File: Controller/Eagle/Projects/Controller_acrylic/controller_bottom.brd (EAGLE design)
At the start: 280.8 x 115 mm, 4 parts

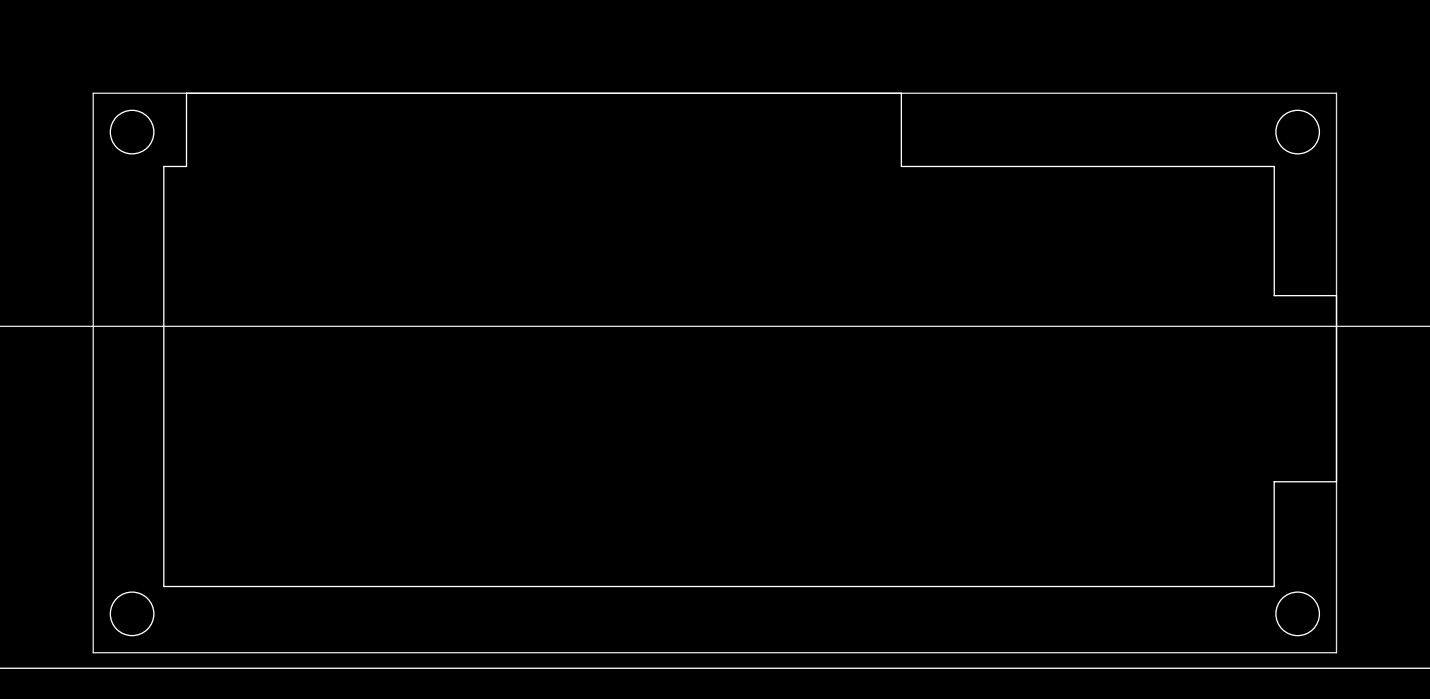
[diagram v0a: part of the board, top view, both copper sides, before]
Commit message: Now it should be ready controller_bottom was not supposed to have the LCD cutout Added dimension to layer 20 in connector board
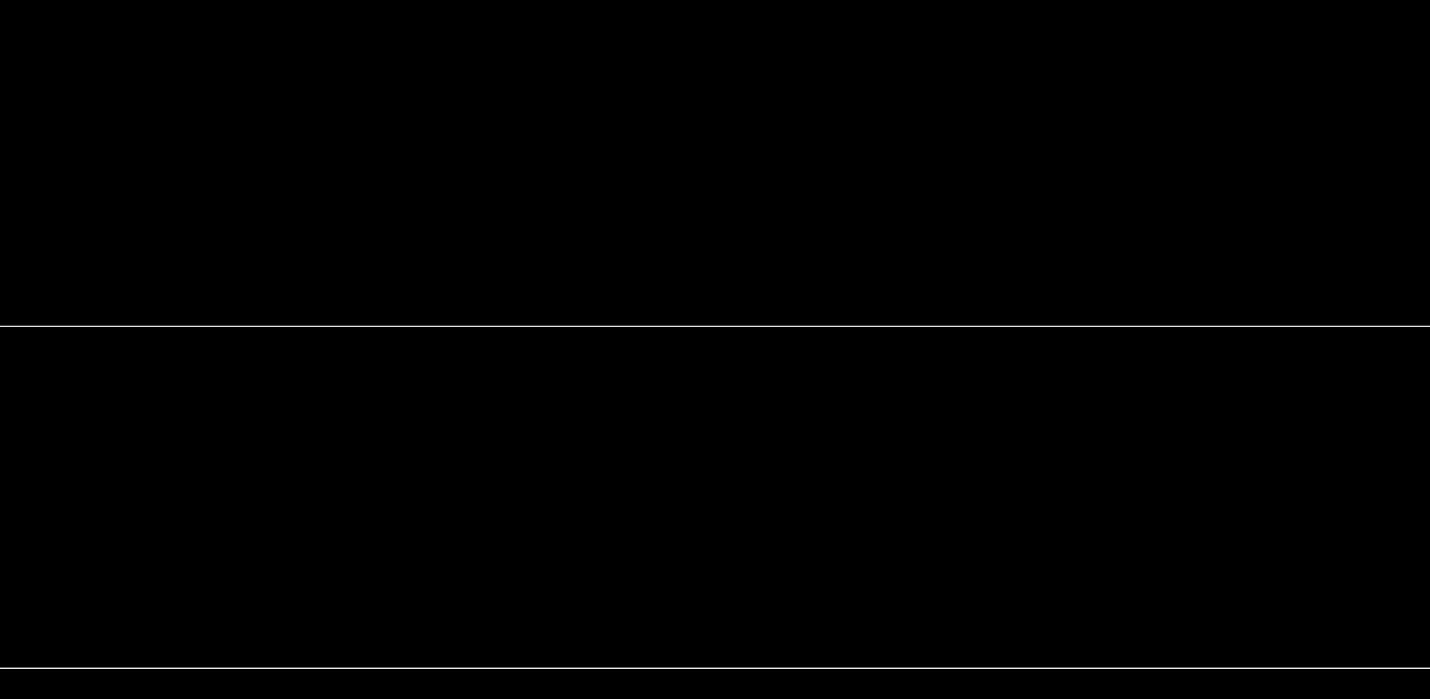
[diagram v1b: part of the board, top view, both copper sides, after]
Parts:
- removed U$4: (no value), Controller:SPARKFUN_LCD_33

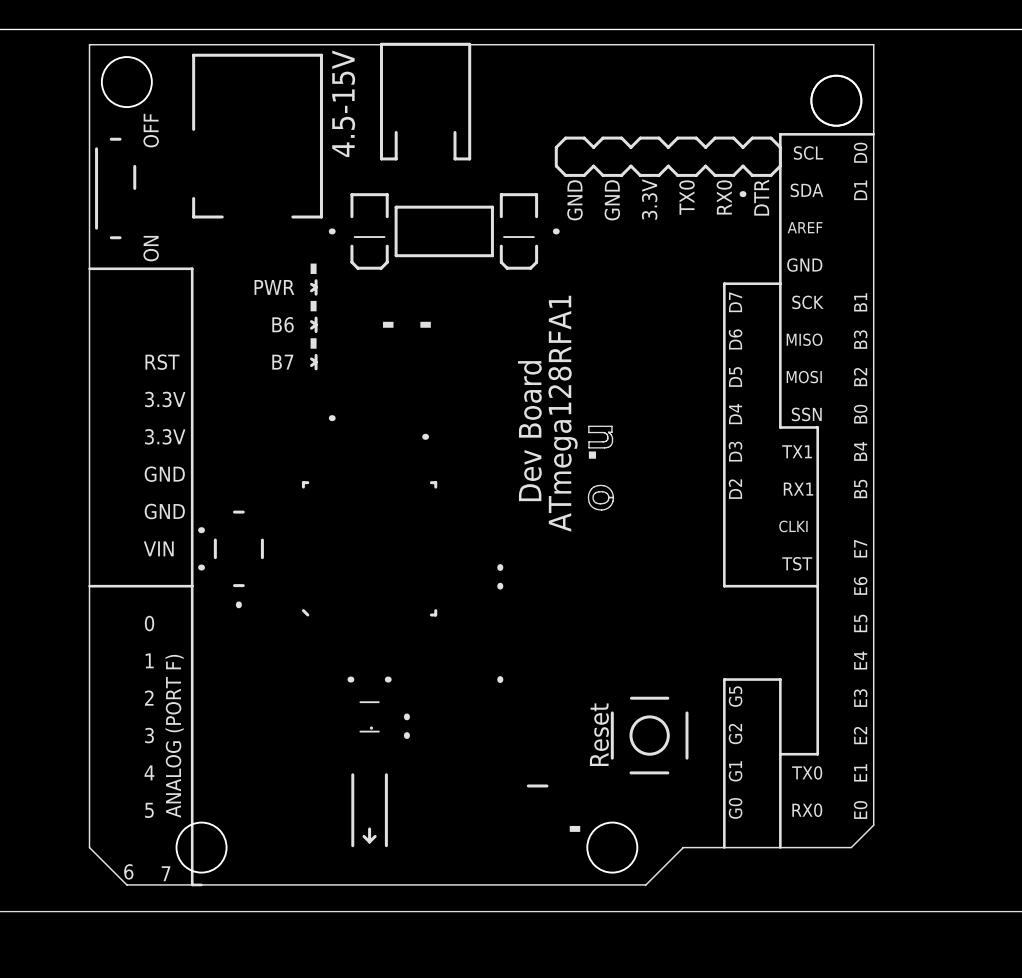
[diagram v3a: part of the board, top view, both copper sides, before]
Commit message: Nudged sparkfun board to the right a bit to make room for battery pack
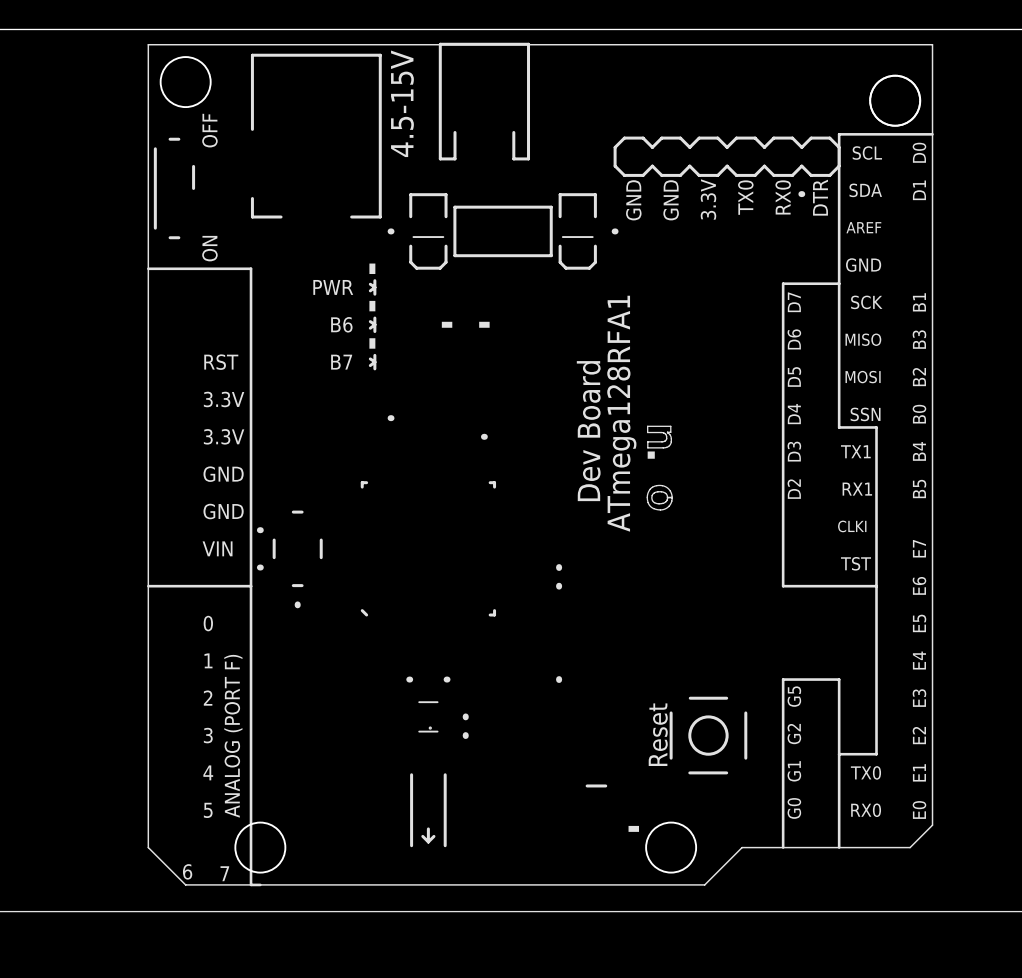
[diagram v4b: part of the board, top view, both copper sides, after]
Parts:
- moved U$3 4.00 mm to (127.9, 114.0)
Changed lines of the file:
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@@
 <layer number="21" name="tPlace" color="7" fill="1" visible="no" active="yes"/>
 <layer number="22" name="bPlace" color="7" fill="1" visible="no" active="yes"/>
-<layer number="23" name="tOrigins" color="15" fill="1" visible="yes" active="yes"/>
+<layer number="23" name="tOrigins" color="15" fill="1" visible="no" active="yes"/>
 <layer number="24" name="bOrigins" color="15" fill="1" visible="no" active="yes"/>
 <layer number="25" name="tNames" color="7" fill="1" visible="no" active="yes"/>
@@
 </autorouter>
 <elements>
-<element name="U$3" library="BOBs" package="ATMEGA128RFA1" value="" x="123.883" y="113.963" rot="R270"/>
+<element name="U$3" library="BOBs" package="ATMEGA128RFA1" value="" x="127.883" y="113.963" rot="R270"/>
 <element name="U$5" library="Controller" package="CONTROLLER_OUTLINE" value="" x="0" y="0"/>
 <element name="U$6" library="Controller" package="CONNECTOR_BOARD_OUTLINE" value="" x="0" y="0"/>
